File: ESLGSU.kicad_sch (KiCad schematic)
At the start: 0 parts

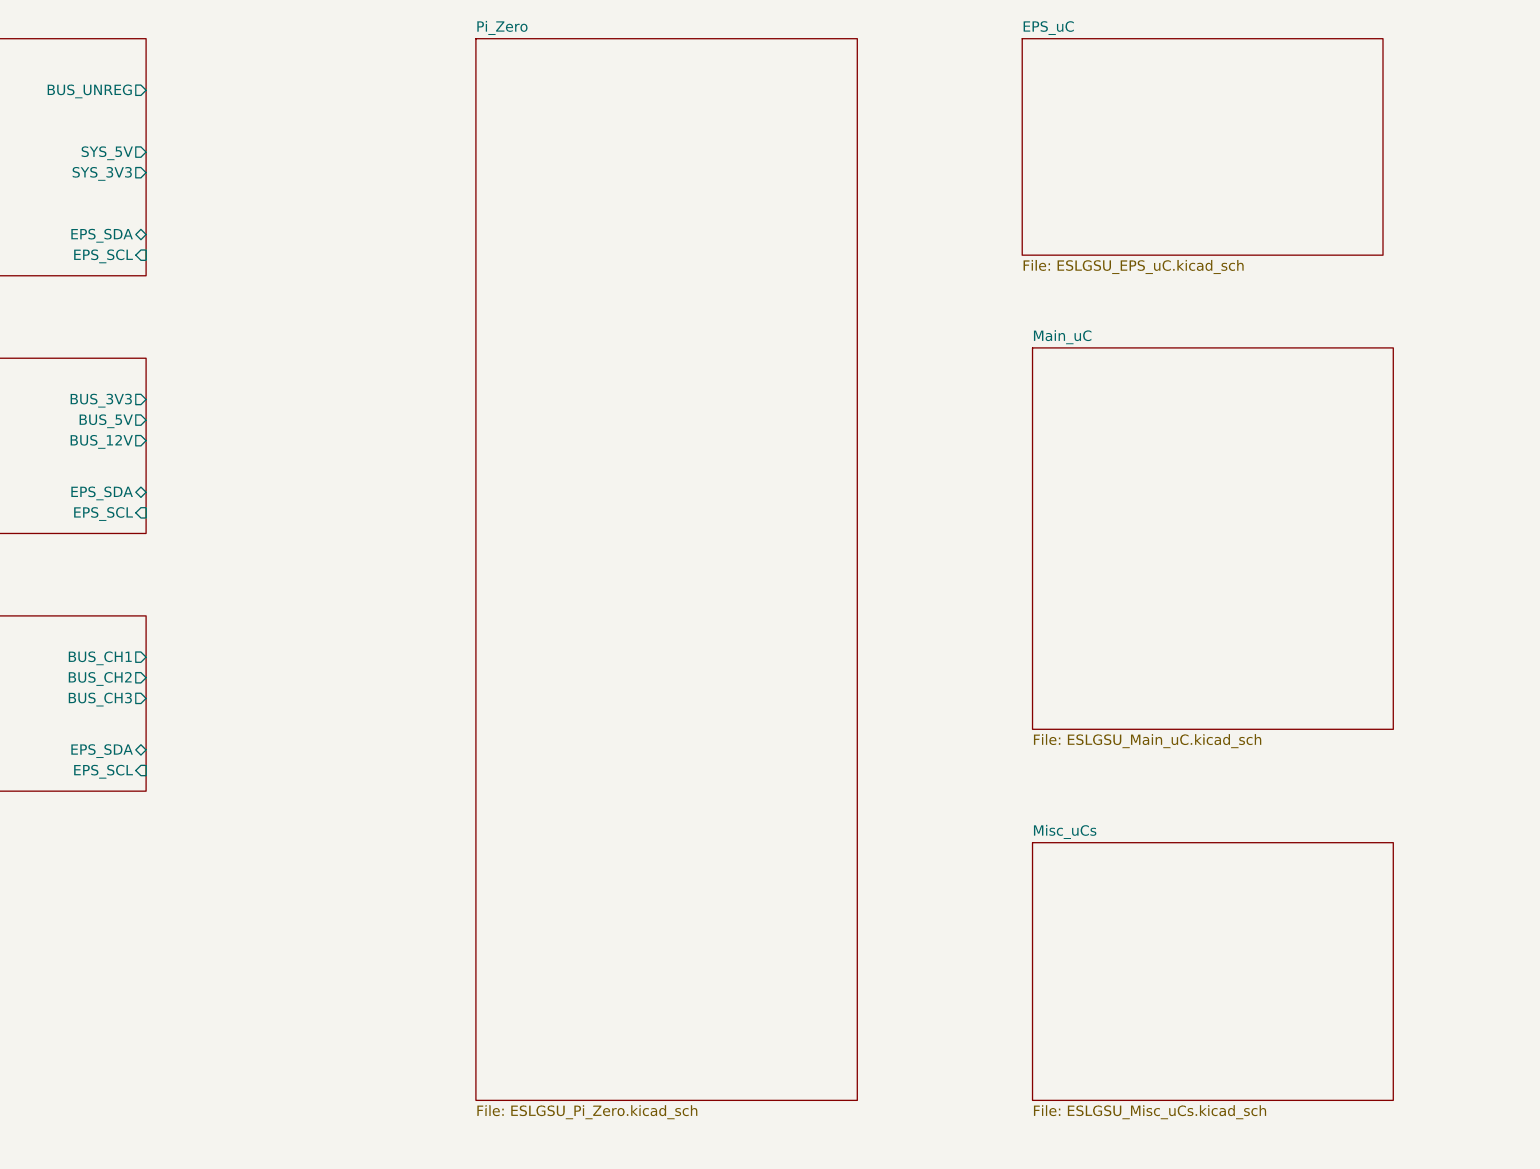
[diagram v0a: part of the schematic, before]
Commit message: Added Pi Zero W 2, continued with schematics
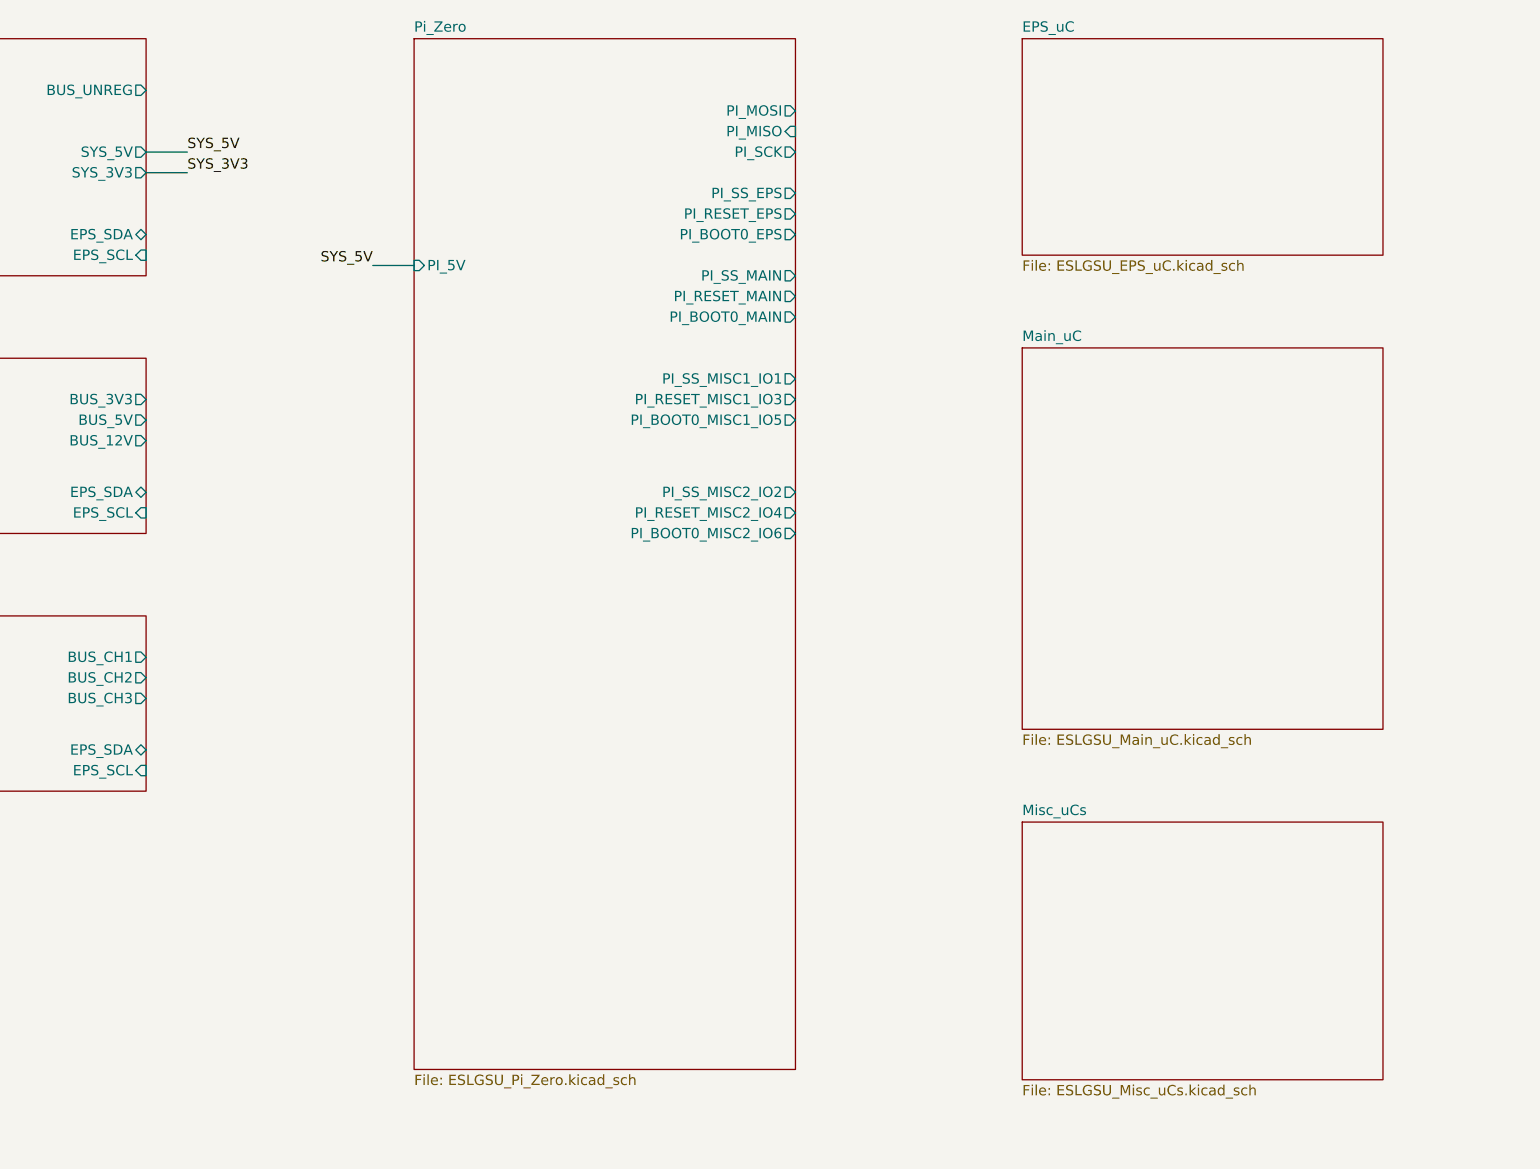
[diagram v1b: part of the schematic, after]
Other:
- sheet Pi_Zero ports: added PI_5V, PI_BOOT0_EPS, PI_BOOT0_MAIN, PI_BOOT0_MISC1_IO5, PI_BOOT0_MISC2_IO6, PI_MISO, PI_MOSI, PI_RESET_EPS, PI_RESET_MAIN, PI_RESET_MISC1_IO3, PI_RESET_MISC2_IO4, PI_SCK, PI_SS_EPS, PI_SS_MAIN, PI_SS_MISC1_IO1, PI_SS_MISC2_IO2; removed none
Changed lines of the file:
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@@
     (company "Electronic Systems Laboratory")
+  )
+  (wire (pts (xy 119.38 41.91) (xy 124.46 41.91))
+    (stroke (width 0) (type default))
+  )
+  (wire (pts (xy 147.32 53.34) (xy 152.4 53.34))
+    (stroke (width 0) (type default))
+  )
+  (wire (pts (xy 119.38 39.37) (xy 124.46 39.37))
+    (stroke (width 0) (type default))
+  )
+  (label "SYS_5V" (at 124.46 39.37 0) (fields_autoplaced)
+    (effects (font (size 1.27 1.27)) (justify left bottom))
+  )
+  (label "SYS_3V3" (at 124.46 41.91 0) (fields_autoplaced)
+    (effects (font (size 1.27 1.27)) (justify left bottom))
+  )
+  (label "SYS_5V" (at 147.32 53.34 180) (fields_autoplaced)
+    (effects (font (size 1.27 1.27)) (justify right bottom))
   )
   (sheet (at 26.67 64.77) (size 92.71 21.59) (fields_autoplaced)
@@
     )
   )
-  (sheet (at 160.02 25.4) (size 46.99 130.81) (fields_autoplaced)
-    (stroke (width 0.1524) (type solid))
-    (fill (color 0 0 0 0.0000))
-    (property "Sheetname" "Pi_Zero" (at 160.02 24.6884 0)
-      (effects (font (size 1.27 1.27)) (justify left bottom))
-    )
-    (property "Sheetfile" "ESLGSU_Pi_Zero.kicad_sch" (at 160.02 156.7946 0)
-      (effects (font (size 1.27 1.27)) (justify left top))
+  (sheet (at 152.4 25.4) (size 46.99 127) (fields_autoplaced)
+    (stroke (width 0.1524) (type solid))
+    (fill (color 0 0 0 0.0000))
+    (property "Sheetname" "Pi_Zero" (at 152.4 24.6884 0)
+      (effects (font (size 1.27 1.27)) (justify left bottom))
+    )
+    (property "Sheetfile" "ESLGSU_Pi_Zero.kicad_sch" (at 152.4 152.9846 0)
+      (effects (font (size 1.27 1.27)) (justify left top))
+    )
+    (pin "PI_BOOT0_EPS" output (at 199.39 49.53 0)
+      (effects (font (size 1.27 1.27)) (justify right))
+    )
+    (pin "PI_BOOT0_MAIN" output (at 199.39 59.69 0)
+      (effects (font (size 1.27 1.27)) (justify right))
+    )
+    (pin "PI_BOOT0_MISC1_IO5" output (at 199.39 72.39 0)
+      (effects (font (size 1.27 1.27)) (justify right))
+    )
+    (pin "PI_RESET_MISC2_IO4" output (at 199.39 83.82 0)
+      (effects (font (size 1.27 1.27)) (justify right))
+    )
+    (pin "PI_BOOT0_MISC2_IO6" output (at 199.39 86.36 0)
+      (effects (font (size 1.27 1.27)) (justify right))
+    )
+    (pin "PI_5V" input (at 152.4 53.34 180)
+      (effects (font (size 1.27 1.27)) (justify left))
+    )
+    (pin "PI_SCK" output (at 199.39 39.37 0)
+      (effects (font (size 1.27 1.27)) (justify right))
+    )
+    (pin "PI_MISO" input (at 199.39 36.83 0)
+      (effects (font (size 1.27 1.27)) (justify right))
+    )
+    (pin "PI_RESET_MAIN" output (at 199.39 57.15 0)
+      (effects (font (size 1.27 1.27)) (justify right))
+    )
+    (pin "PI_MOSI" output (at 199.39 34.29 0)
+      (effects (font (size 1.27 1.27)) (justify right))
+    )
+    (pin "PI_RESET_MISC1_IO3" output (at 199.39 69.85 0)
+      (effects (font (size 1.27 1.27)) (justify right))
+    )
+    (pin "PI_SS_EPS" output (at 199.39 44.45 0)
+      (effects (font (size 1.27 1.27)) (justify right))
+    )
+    (pin "PI_SS_MAIN" output (at 199.39 54.61 0)
+      (effects (font (size 1.27 1.27)) (justify right))
+    )
+    (pin "PI_SS_MISC2_IO2" output (at 199.39 81.28 0)
+      (effects (font (size 1.27 1.27)) (justify right))
+    )
+    (pin "PI_SS_MISC1_IO1" output (at 199.39 67.31 0)
+      (effects (font (size 1.27 1.27)) (justify right))
+    )
+    (pin "PI_RESET_EPS" output (at 199.39 46.99 0)
+      (effects (font (size 1.27 1.27)) (justify right))
     )
     (instances
@@
     )
   )
-  (sheet (at 228.6 63.5) (size 44.45 46.99) (fields_autoplaced)
-    (stroke (width 0.1524) (type solid))
-    (fill (color 0 0 0 0.0000))
-    (property "Sheetname" "Main_uC" (at 228.6 62.7884 0)
-      (effects (font (size 1.27 1.27)) (justify left bottom))
-    )
-    (property "Sheetfile" "ESLGSU_Main_uC.kicad_sch" (at 228.6 111.0746 0)
+  (sheet (at 227.33 63.5) (size 44.45 46.99) (fields_autoplaced)
+    (stroke (width 0.1524) (type solid))
+    (fill (color 0 0 0 0.0000))
+    (property "Sheetname" "Main_uC" (at 227.33 62.7884 0)
+      (effects (font (size 1.27 1.27)) (justify left bottom))
+    )
+    (property "Sheetfile" "ESLGSU_Main_uC.kicad_sch" (at 227.33 111.0746 0)
       (effects (font (size 1.27 1.27)) (justify left top))
     )
@@
     )
   )
-  (sheet (at 228.6 124.46) (size 44.45 31.75) (fields_autoplaced)
-    (stroke (width 0.1524) (type solid))
-    (fill (color 0 0 0 0.0000))
-    (property "Sheetname" "Misc_uCs" (at 228.6 123.7484 0)
-      (effects (font (size 1.27 1.27)) (justify left bottom))
-    )
-    (property "Sheetfile" "ESLGSU_Misc_uCs.kicad_sch" (at 228.6 156.7946 0)
-      (effects (font (size 1.27 1.27)) (justify left top))
-    )
+  (sheet (at 227.33 121.92) (size 44.45 31.75) (fields_autoplaced)
+    (stroke (width 0.1524) (type solid))
+    (fill (color 0 0 0 0.0000))
+    (property "Sheetname" "Misc_uCs" (at 227.33 121.2084 0)
+      (effects (font (size 1.27 1.27)) (justify left bottom))
+    )
+    (property "Sheetfile" "ESLGSU_Misc_uCs.kicad_sch" (at 227.33 154.2546 0)
+      (effects (font (size 1.27 1.27)) (justify left top))
+    )

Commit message: Started work on system power section
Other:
- sheet Pi_Zero ports: added PI_I2C_SCL, PI_I2C_SDA, PI_UART_RX, PI_UART_TX; removed none

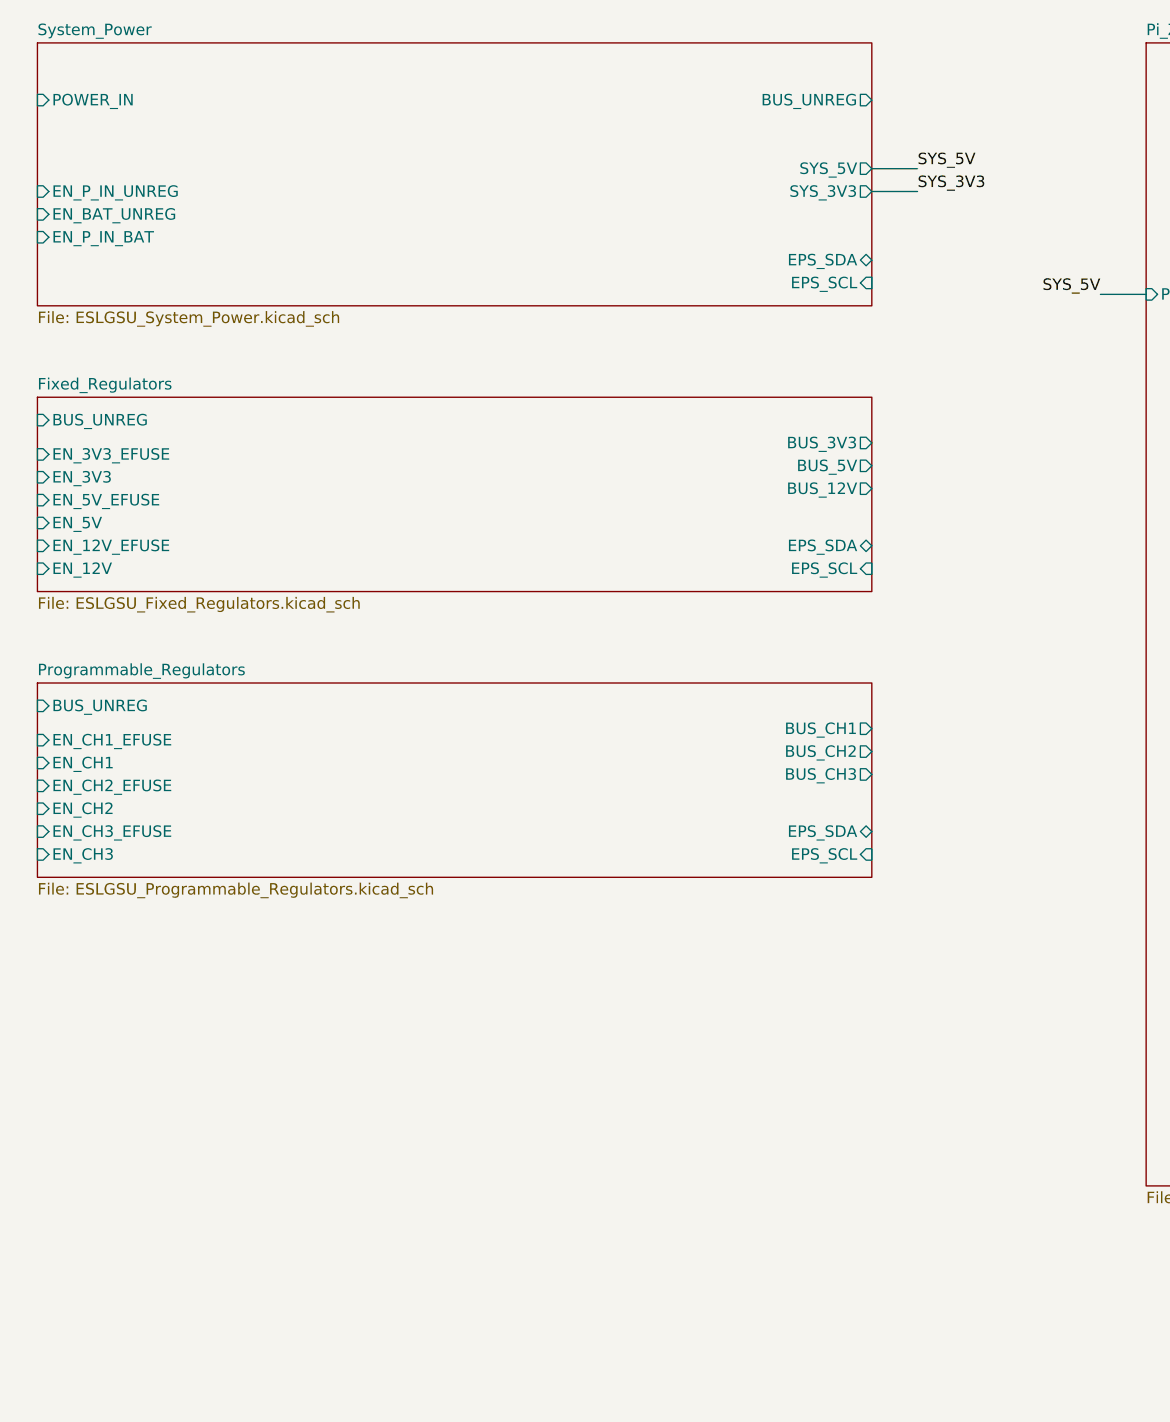
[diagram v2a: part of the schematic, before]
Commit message: Additional power regulation work
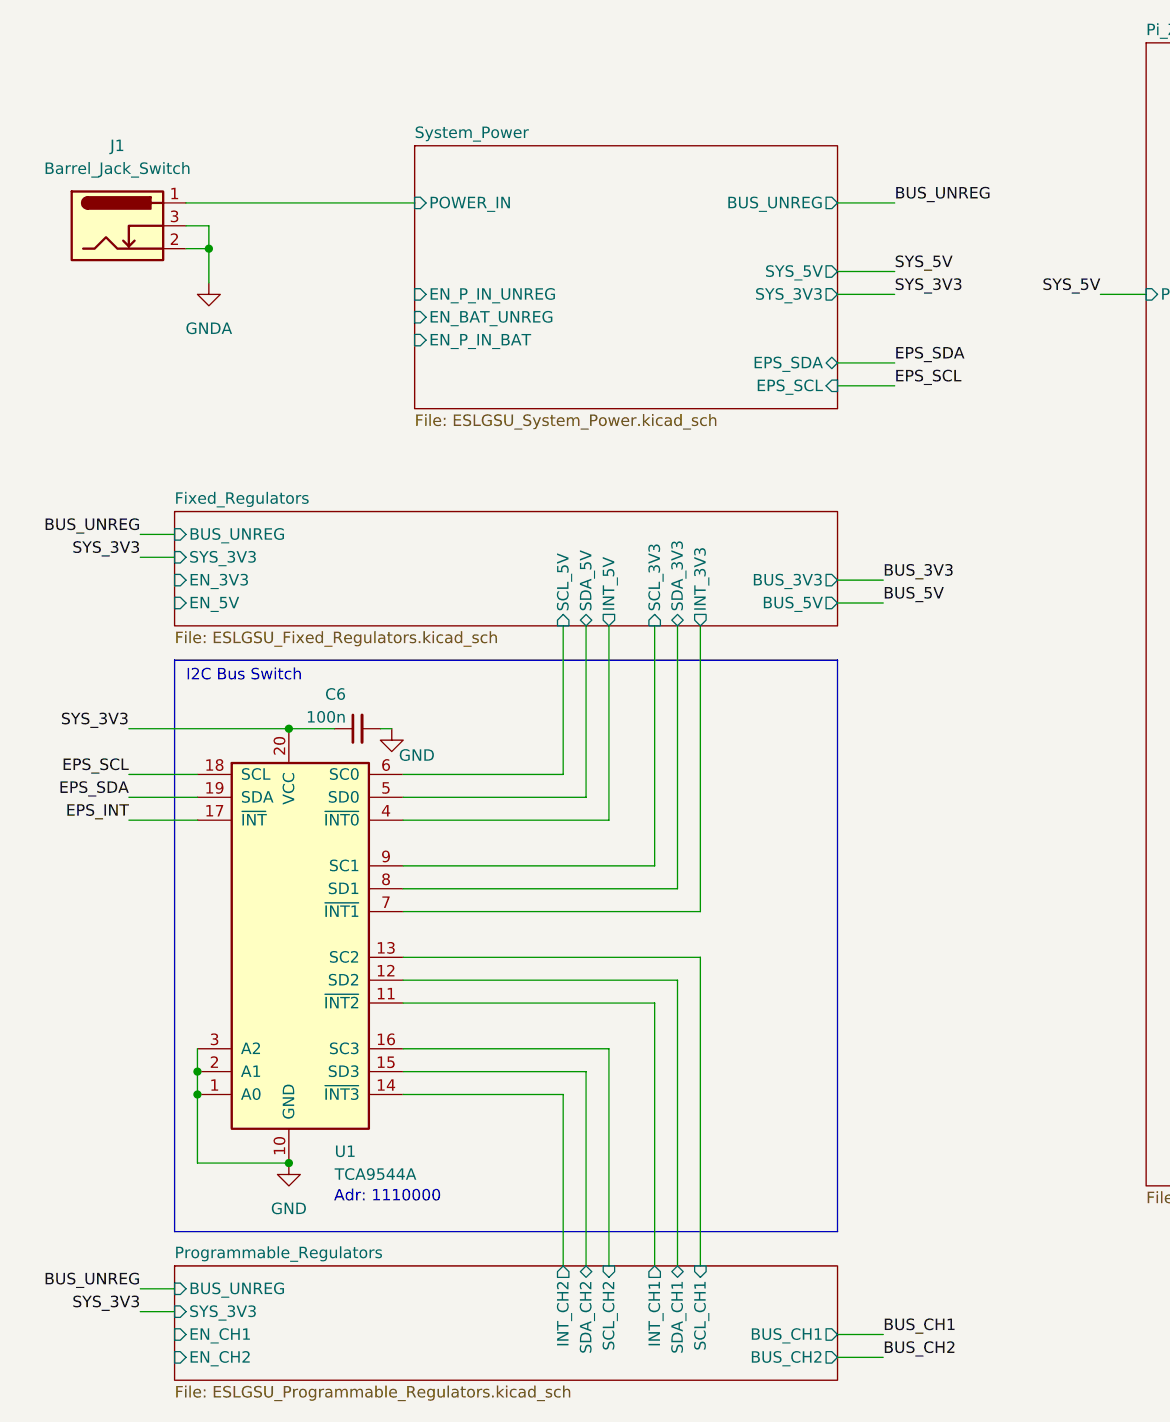
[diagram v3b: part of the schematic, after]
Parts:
- added C6: 100n, Capacitor_SMD:C_0603_1608Metric, symbol Device:C_Small
- added J1: Barrel_Jack_Switch, ESLGSU_Parts_Lib:PJ-082BH, symbol Connector:Barrel_Jack_Switch
- added U1: TCA9544A, Package_SO:TSSOP-20_4.4x6.5mm_P0.65mm, symbol Interface_Expansion:TCA9544A
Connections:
- net SYS_3V3: now also C6.1, U1.20 (VCC)
- net System_Power/POWER_IN: now also J1.1
- new net EPS_INT: U1.17 (~{INT})
- new net EPS_SCL: U1.18 (SCL)
- new net EPS_SDA: U1.19 (SDA)
- new net Fixed_Regulators/INT_3V3: U1.7 (~{INT1})
- new net Fixed_Regulators/INT_5V: U1.4 (~{INT0})
- new net Fixed_Regulators/SCL_3V3: U1.9 (SC1)
- new net Fixed_Regulators/SCL_5V: U1.6 (SC0)
- new net Fixed_Regulators/SDA_3V3: U1.8 (SD1)
- new net Fixed_Regulators/SDA_5V: U1.5 (SD0)
- new net GND: C6.2, U1.1 (A0), U1.10 (GND), U1.2 (A1), U1.3 (A2)
- new net GNDA: J1.2, J1.3
- new net Programmable_Regulators/INT_CH1: U1.11 (~{INT2})
- new net Programmable_Regulators/INT_CH2: U1.14 (~{INT3})
- new net Programmable_Regulators/SCL_CH1: U1.13 (SC2)
- new net Programmable_Regulators/SCL_CH2: U1.16 (SC3)
- new net Programmable_Regulators/SDA_CH1: U1.12 (SD2)
- new net Programmable_Regulators/SDA_CH2: U1.15 (SD3)
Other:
- sheet Fixed_Regulators ports: added INT_3V3, INT_5V, SCL_3V3, SCL_5V, SDA_3V3, SDA_5V, SYS_3V3; removed BUS_12V, EN_12V, EN_12V_EFUSE, EN_3V3_EFUSE, EN_5V_EFUSE, EPS_SCL, EPS_SDA
- sheet Programmable_Regulators ports: added INT_CH1, INT_CH2, SCL_CH1, SCL_CH2, SDA_CH1, SDA_CH2, SYS_3V3; removed BUS_CH3, EN_CH1_EFUSE, EN_CH2_EFUSE, EN_CH3, EN_CH3_EFUSE, EPS_SCL, EPS_SDA
- note added: "Adr: 1110000"
- note added: "I2C Bus Switch"
